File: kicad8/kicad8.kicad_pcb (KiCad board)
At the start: 2 copper layers, 314.5 x 124 mm, 192 parts, among them J1 USB_C_Receptacle_USB2.0, SW1 RotaryEncoder_Switch, U1 STM32F072CBT6, U2 PRTR5V0U2X, U3 XC6206PxxxMR-Regulator_Linear

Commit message: Added: Stepped CAPS_LOCK and Split backspace
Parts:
- removed the MX76 at (50.9, 124.8)
- removed the MX77 at (74.7, 124.8)
- added D29: D_Small, Diode_SMD:D_SOD-123, B.Cu at (269.1, 47.4)
- added MX28: MX_SW_solder, PCM_marbastlib-mx:SW_MX_1u, F.Cu at (272.3, 48.6)
- added MX30: MX_SW_solder, PCM_marbastlib-mx:SW_MX_1u, F.Cu at (291.4, 48.6)
- added MX48: MX_SW_HS, PCM_marbastlib-mx:SW_MX_HS_S_CPG151101S11_1u, B.Cu at (27.1, 86.7)
- added MX78: MX_SW_HS, PCM_marbastlib-mx:SW_MX_HS_CPG151101S11_1.25u, B.Cu at (50.9, 124.8)
- added MX79: MX_SW_HS, PCM_marbastlib-mx:SW_MX_HS_CPG151101S11_1.25u, B.Cu at (74.7, 124.8)
- added MX87: MX_SW_HS, PCM_marbastlib-mx:SW_MX_HS_CPG151101S11_1u, B.Cu at (320.0, 24.7)
- added R5: 500, Diode_SMD:D_SOD-123, F.Cu at (340.1, 15.2)
- added R6: 10k, Diode_SMD:D_SOD-123, B.Cu at (309.2, 26.8)
- added RDB_UL_1: WS2812B, LED_SMD:LED_WS2812B_PLCC4_5.0x5.0mm_P3.2mm, F.Cu at (341.3, 22.0)
- added RDB_UL_10: WS2812B, LED_SMD:LED_WS2812B_PLCC4_5.0x5.0mm_P3.2mm, F.Cu at (349.7, 28.7)
- added RDB_UL_11: WS2812B, LED_SMD:LED_WS2812B_PLCC4_5.0x5.0mm_P3.2mm, F.Cu at (349.7, 35.3)
- added RDB_UL_12: WS2812B, LED_SMD:LED_WS2812B_PLCC4_5.0x5.0mm_P3.2mm, F.Cu at (349.7, 41.9)
- added RDB_UL_13: WS2812B, LED_SMD:LED_WS2812B_PLCC4_5.0x5.0mm_P3.2mm, F.Cu at (349.7, 48.5)
- added RDB_UL_14: WS2812B, LED_SMD:LED_WS2812B_PLCC4_5.0x5.0mm_P3.2mm, F.Cu at (349.7, 55.1)
- added RDB_UL_15: WS2812B, LED_SMD:LED_WS2812B_PLCC4_5.0x5.0mm_P3.2mm, F.Cu at (349.7, 61.8)
- added RDB_UL_16: WS2812B, LED_SMD:LED_WS2812B_PLCC4_5.0x5.0mm_P3.2mm, F.Cu at (349.7, 68.4)
- added RDB_UL_17: WS2812B, LED_SMD:LED_WS2812B_PLCC4_5.0x5.0mm_P3.2mm, F.Cu at (358.1, 22.0)
- added RDB_UL_18: WS2812B, LED_SMD:LED_WS2812B_PLCC4_5.0x5.0mm_P3.2mm, F.Cu at (358.1, 28.7)
- added RDB_UL_19: WS2812B, LED_SMD:LED_WS2812B_PLCC4_5.0x5.0mm_P3.2mm, F.Cu at (358.1, 35.3)
- added RDB_UL_2: WS2812B, LED_SMD:LED_WS2812B_PLCC4_5.0x5.0mm_P3.2mm, F.Cu at (341.3, 28.7)
- added RDB_UL_20: WS2812B, LED_SMD:LED_WS2812B_PLCC4_5.0x5.0mm_P3.2mm, F.Cu at (358.1, 41.9)
- added RDB_UL_21: WS2812B, LED_SMD:LED_WS2812B_PLCC4_5.0x5.0mm_P3.2mm, F.Cu at (358.1, 48.5)
- added RDB_UL_22: WS2812B, LED_SMD:LED_WS2812B_PLCC4_5.0x5.0mm_P3.2mm, F.Cu at (358.1, 55.1)
- added RDB_UL_23: WS2812B, LED_SMD:LED_WS2812B_PLCC4_5.0x5.0mm_P3.2mm, F.Cu at (358.1, 61.8)
- added RDB_UL_24: WS2812B, LED_SMD:LED_WS2812B_PLCC4_5.0x5.0mm_P3.2mm, F.Cu at (358.1, 68.4)
- added RDB_UL_25: WS2812B, LED_SMD:LED_WS2812B_PLCC4_5.0x5.0mm_P3.2mm, F.Cu at (366.5, 22.0)
- added RDB_UL_26: WS2812B, LED_SMD:LED_WS2812B_PLCC4_5.0x5.0mm_P3.2mm, F.Cu at (366.5, 28.7)
- added RDB_UL_27: WS2812B, LED_SMD:LED_WS2812B_PLCC4_5.0x5.0mm_P3.2mm, F.Cu at (366.5, 35.3)
- added RDB_UL_28: WS2812B, LED_SMD:LED_WS2812B_PLCC4_5.0x5.0mm_P3.2mm, F.Cu at (366.5, 41.9)
- added RDB_UL_29: WS2812B, LED_SMD:LED_WS2812B_PLCC4_5.0x5.0mm_P3.2mm, F.Cu at (366.5, 48.5)
- added RDB_UL_3: WS2812B, LED_SMD:LED_WS2812B_PLCC4_5.0x5.0mm_P3.2mm, F.Cu at (341.3, 35.3)
- added RDB_UL_30: WS2812B, LED_SMD:LED_WS2812B_PLCC4_5.0x5.0mm_P3.2mm, F.Cu at (366.5, 55.1)
- added RDB_UL_31: WS2812B, LED_SMD:LED_WS2812B_PLCC4_5.0x5.0mm_P3.2mm, F.Cu at (366.5, 61.8)
- added RDB_UL_32: WS2812B, LED_SMD:LED_WS2812B_PLCC4_5.0x5.0mm_P3.2mm, F.Cu at (366.5, 68.4)
- added RDB_UL_33: WS2812B, LED_SMD:LED_WS2812B_PLCC4_5.0x5.0mm_P3.2mm, F.Cu at (374.9, 22.0)
- added RDB_UL_34: WS2812B, LED_SMD:LED_WS2812B_PLCC4_5.0x5.0mm_P3.2mm, F.Cu at (374.9, 28.7)
- added RDB_UL_35: WS2812B, LED_SMD:LED_WS2812B_PLCC4_5.0x5.0mm_P3.2mm, F.Cu at (374.9, 35.3)
- added RDB_UL_36: WS2812B, LED_SMD:LED_WS2812B_PLCC4_5.0x5.0mm_P3.2mm, F.Cu at (374.9, 41.9)
- added RDB_UL_37: WS2812B, LED_SMD:LED_WS2812B_PLCC4_5.0x5.0mm_P3.2mm, F.Cu at (374.9, 48.5)
- added RDB_UL_38: WS2812B, LED_SMD:LED_WS2812B_PLCC4_5.0x5.0mm_P3.2mm, F.Cu at (374.9, 55.1)
- added RDB_UL_4: WS2812B, LED_SMD:LED_WS2812B_PLCC4_5.0x5.0mm_P3.2mm, F.Cu at (341.3, 41.9)
- added RDB_UL_5: WS2812B, LED_SMD:LED_WS2812B_PLCC4_5.0x5.0mm_P3.2mm, F.Cu at (341.3, 48.5)
- added RDB_UL_6: WS2812B, LED_SMD:LED_WS2812B_PLCC4_5.0x5.0mm_P3.2mm, F.Cu at (341.3, 55.1)
- added RDB_UL_7: WS2812B, LED_SMD:LED_WS2812B_PLCC4_5.0x5.0mm_P3.2mm, F.Cu at (341.3, 61.8)
- added RDB_UL_8: WS2812B, LED_SMD:LED_WS2812B_PLCC4_5.0x5.0mm_P3.2mm, F.Cu at (341.3, 68.4)
- added RDB_UL_9: WS2812B, LED_SMD:LED_WS2812B_PLCC4_5.0x5.0mm_P3.2mm, F.Cu at (349.7, 22.0)
- MX32: renamed from MX31; footprint PCM_marbastlib-mx:SW_MX_HS_CPG151101S11_1u -> PCM_marbastlib-mx:SW_MX_HS_CPG151101S11_1.5u
- MX45: renamed from MX44; footprint PCM_marbastlib-mx:SW_MX_HS_CPG151101S11_1u -> PCM_marbastlib-mx:SW_MX_HS_CPG151101S11_1.5u
- MX74: renamed from MX72; footprint PCM_marbastlib-mx:SW_MX_HS_CPG151101S11_1u -> PCM_marbastlib-mx:SW_MX_HS_CPG151101S11_1.75u
- MX77: renamed from MX75; footprint PCM_marbastlib-mx:SW_MX_HS_CPG151101S11_1u -> PCM_marbastlib-mx:SW_MX_HS_CPG151101S11_1.25u
- SW1: value RotaryEncoder_Switch -> ROT_SKYLOONG_HS; footprint PCM_marbastlib-various:ROT_Alps_EC11E-Switch -> PCM_marbastlib-various:ROT_SKYLOONG_HS-Switch
- moved C1 34.2 mm to (308.8, 108.5)
- moved R4 34.2 mm to (309.1, 110.7)
- moved BOOT1 34.2 mm to (313.6, 116.8)
- moved RST1 34.2 mm to (307.3, 116.8)
- moved R3 34.1 mm to (311.3, 110.7)
- moved C2 15.6 mm to (315.6, 58.5), turned to 90 degrees
- moved C4 15.5 mm to (307.0, 51.9), turned to 45 degrees
- moved C3 11.3 mm to (313.2, 58.1), turned to -45 degrees
- moved D47 9.80 mm to (44.6, 89.2), turned to 180 degrees
- moved D15 9.72 mm to (309.2, 21.2), turned to 90 degrees
- moved D59 9.65 mm to (273.1, 89.5), turned to 0 degrees
- moved C7 7.94 mm to (301.3, 61.9), turned to -45 degrees
- moved U1 6.40 mm to (307.1, 58.3), turned to 45 degrees
- moved D30 6.40 mm to (280.2, 53.7), turned to 0 degrees
- moved D28 5.16 mm to (256.4, 54.5)
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- renumbered D29 to D30, D30 to D31, D31 to D32, D32 to D33, D33 to D34, D34 to D35, D35 to D36, D36 to D37, D37 to D38, D38 to D39, D39 to D40, D40 to D41, D41 to D42, D42 to D43, D43 to D44, D44 to D45, D45 to D46, D46 to D47, D47 to D48, D48 to D49, D49 to D50, D50 to D51, D51 to D52, D52 to D53, D53 to D54, D54 to D55, D55 to D56, D56 to D57, D57 to D58, D58 to D59, D59 to D60, D60 to D61, D61 to D62, D62 to D63, D63 to D64, D64 to D65, D65 to D66, D66 to D67, D67 to D68, D68 to D69, D69 to D70, D70 to D71, D71 to D72, D72 to D73, D73 to D74, D74 to D75, D75 to D76, D76 to D77, D77 to D78, D78 to D79, D79 to D80, D80 to D81, D81 to D82, D82 to D83, D83 to D84, D84 to D85, MX16 to MX15, MX17 to MX16, MX18 to MX17, MX19 to MX18, MX20 to MX19, MX21 to MX20, MX22 to MX21, MX23 to MX22, MX24 to MX23, MX25 to MX24, MX26 to MX25, MX27 to MX26, MX28 to MX27, MX30 to MX31, MX32 to MX33, MX33 to MX34, MX34 to MX35, MX35 to MX36, MX36 to MX37, MX37 to MX38, MX38 to MX39, MX39 to MX40, MX40 to MX41, MX41 to MX42, MX42 to MX43, MX43 to MX44, MX45 to MX46, MX46 to MX47, MX47 to MX49, MX48 to MX50, MX49 to MX51, MX50 to MX52, MX51 to MX53, MX52 to MX54, MX53 to MX55, MX54 to MX56, MX55 to MX57, MX56 to MX58, MX57 to MX59, MX58 to MX60, MX59 to MX61, MX60 to MX62, MX61 to MX63, MX62 to MX64, MX63 to MX65, MX64 to MX66, MX65 to MX67, MX66 to MX68, MX67 to MX69, MX68 to MX70, MX69 to MX71, MX70 to MX72, MX71 to MX73, MX73 to MX75, MX74 to MX76, MX78 to MX80, MX79 to MX81, MX80 to MX82, MX81 to MX83, MX82 to MX84, MX83 to MX85, MX84 to MX86, S58 to S1, S78 to S2
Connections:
- U1 pad 10: col13 -> col10
- U1 pad 11: col11 -> col9
- U1 pad 12: col10 -> row2
- U1 pad 13: col9 -> col8
- U1 pad 14: col8 -> col7
- U1 pad 15: col7 -> col6
- U1 pad 16: col6 -> col5
- U1 pad 17: col5 -> col4
- U1 pad 18: col4 -> col3
- U1 pad 19: col3 -> col2
- U1 pad 2: /C13 -> row4
- U1 pad 20: col2 -> col1
- U1 pad 21: col1 -> col0
- U1 pad 22: col0 -> row0
- U1 pad 25: col12 -> rot1
- U1 pad 26: /B13 -> rot0
- U1 pad 28: /B15 -> row1
- U1 pad 3: row2 -> row3
- U1 pad 37: row0 -> col14
- U1 pad 38: rot1 -> /A15
- U1 pad 39: rot0 -> /B3
- U1 pad 4: row3 -> col13
- U1 pad 40: row1 -> /B4
- U1 pad 43: col14 -> /B7
- U1 pad 46: /B9 -> row5
- U1 pad 5: row4 -> col12
- U1 pad 6: row5 -> col11
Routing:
- net GND: track 166.0 -> 224.5 mm
- net row3: track 318.0 -> 370.7 mm, vias 2 -> 4
- net col0: track 383.3 -> 429.0 mm
- net BOOT0: track 31.9 -> 73.6 mm
- net Net-(D47-A): track 3.67 -> 44.0 mm
- net NRST: track 27.7 -> 67.8 mm, vias 2 -> 4
- net col1: track 365.2 -> 401.6 mm
- net col2: track 348.3 -> 383.9 mm
- net col3: track 307.5 -> 342.4 mm
- net +3V3: track 98.6 -> 133.3 mm, vias 5 -> 8
- net col4: track 288.6 -> 322.8 mm
- net col5: track 269.8 -> 303.2 mm
- net col6: track 271.0 -> 303.6 mm
- net col7: track 234.1 -> 266.0 mm
- net col8: track 215.2 -> 246.4 mm
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
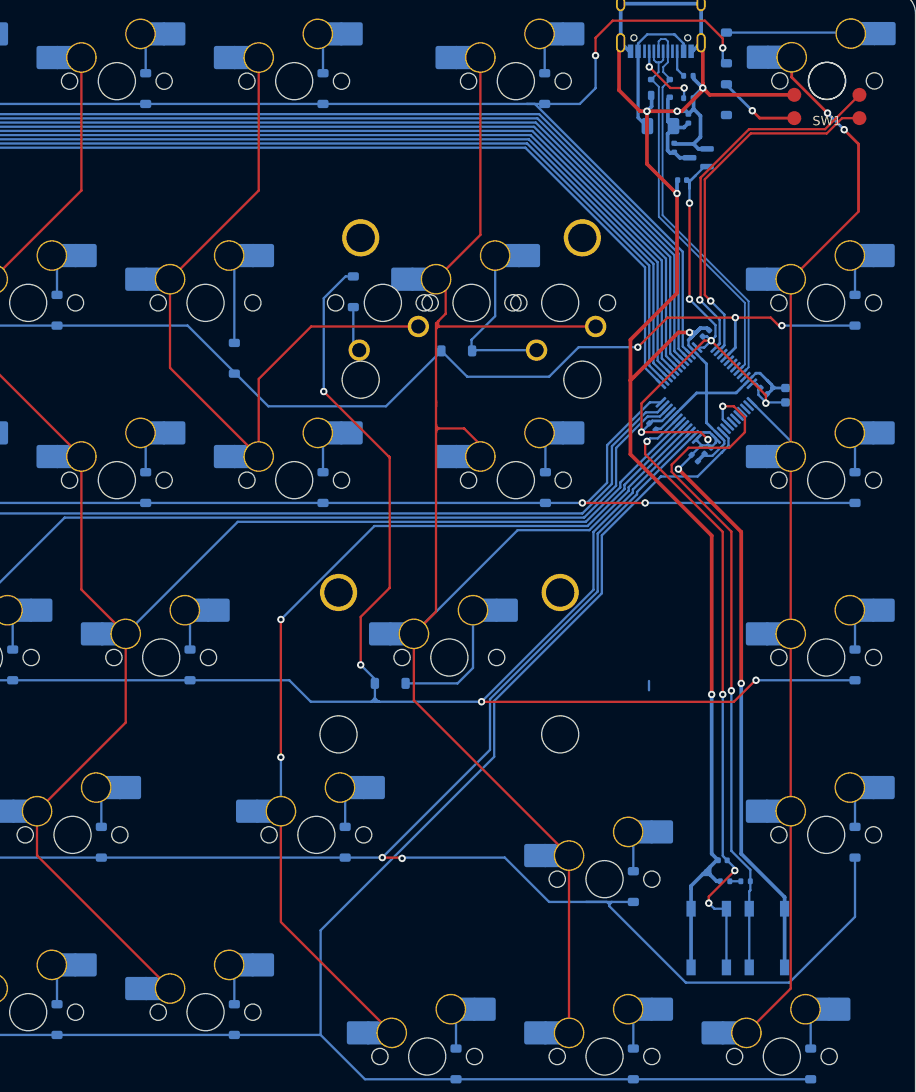
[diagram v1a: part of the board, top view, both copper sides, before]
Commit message: Added: Skyloong rotary encoder
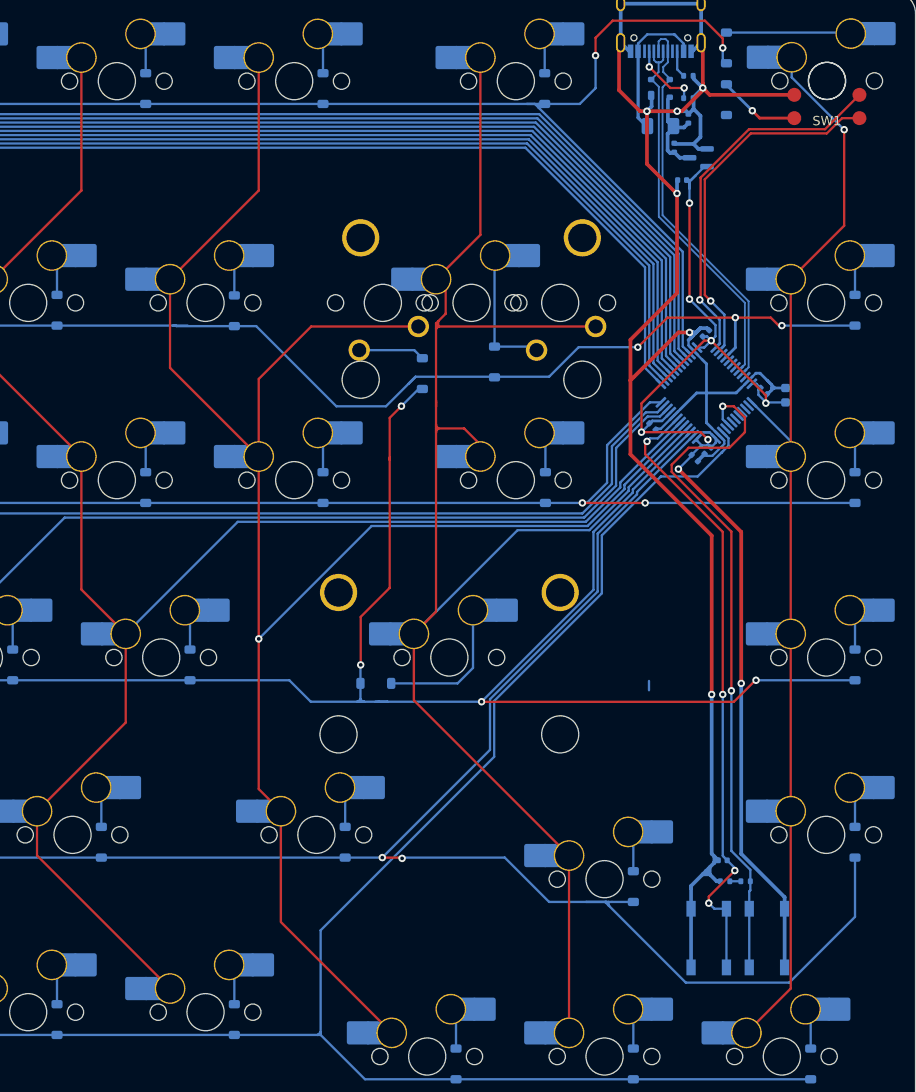
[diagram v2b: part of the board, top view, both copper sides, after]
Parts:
- moved D29 11.5 mm to (276.6, 56.2), turned to 90 degrees
- moved D28 5.10 mm to (256.4, 49.4)
- moved D30 4.23 mm to (284.3, 54.9), turned to 90 degrees
- moved D59 1.55 mm to (271.6, 89.5)
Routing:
- net col12: track 180.1 -> 201.8 mm, vias 2 -> 1
- net row3: track 370.7 -> 356.2 mm
- net Net-(D28-A): track 8.83 -> 4.51 mm
- net Net-(D30-A): track 18.2 -> 14.5 mm
- net Net-(D29-A): track 3.99 -> 7.14 mm
- net Net-(D59-A): track 14.8 -> 16.4 mm
- net col14: track 120.3 -> 119.0 mm, vias 2 -> 1
- net GND: track 224.5 -> 225.3 mm
